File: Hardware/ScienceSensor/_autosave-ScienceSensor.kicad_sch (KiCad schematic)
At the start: 16 parts

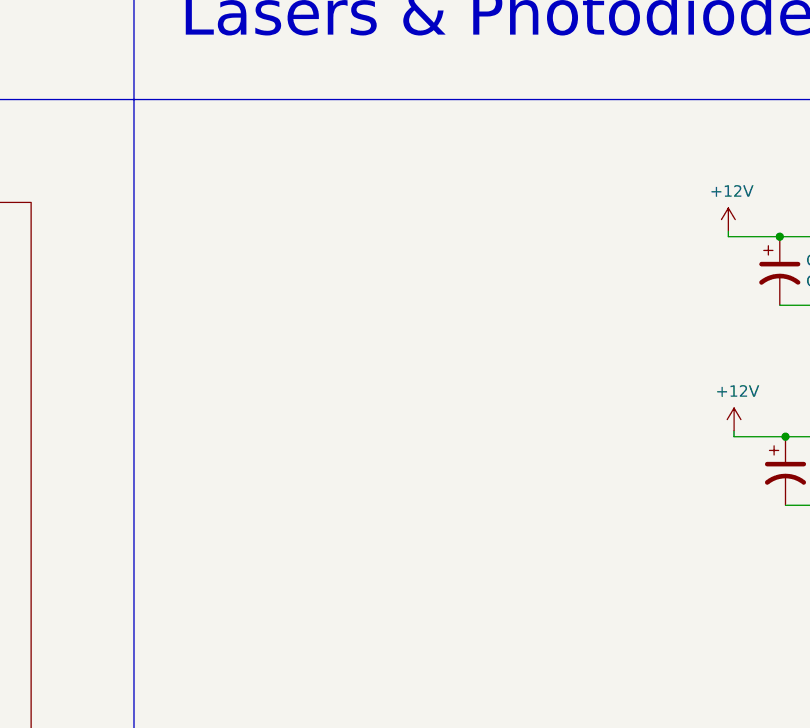
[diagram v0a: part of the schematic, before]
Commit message: Created servo and started limit switch for microscope.
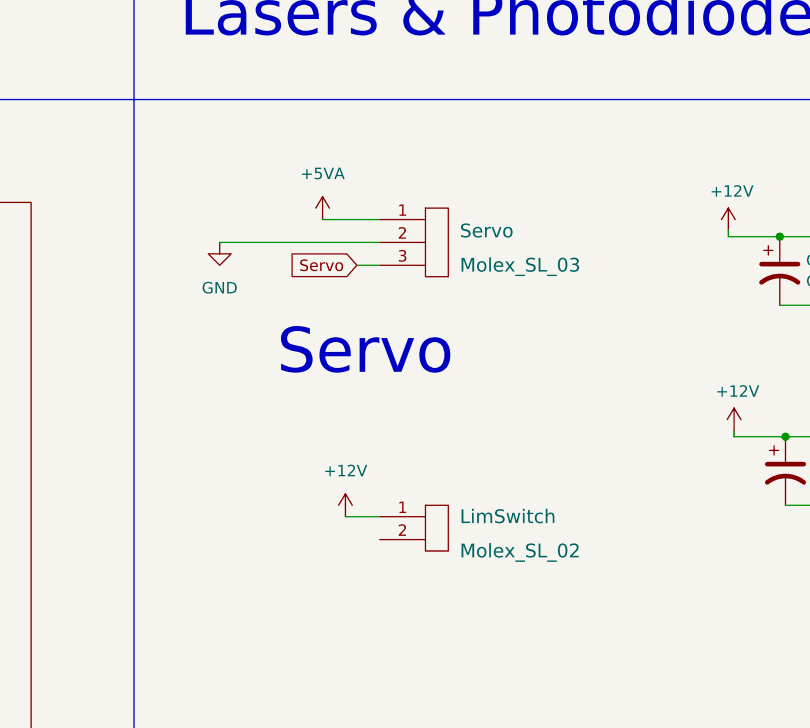
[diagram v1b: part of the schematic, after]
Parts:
- added LimSwitch: Molex_SL_02, symbol MRDT_Connectors:Molex_SL_02
- added Servo: Molex_SL_03, symbol MRDT_Connectors:Molex_SL_03
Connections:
- net +12V: now also LimSwitch.1
- net GND: now also Servo.2
- new net +5VA: Servo.1
- new net Servo: Servo.3
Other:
- note added: "Servo"
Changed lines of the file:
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@@
+    (stroke (width 0) (type default) (color 0 0 0 0))
+  )
+  (wire (pts (xy 140.97 115.57) (xy 147.32 115.57))
     (stroke (width 0) (type default) (color 0 0 0 0))
   )
@@
     (stroke (width 0) (type default) (color 0 0 0 0))
   )
+  (wire (pts (xy 143.51 148.59) (xy 147.32 148.59))
+    (stroke (width 0) (type default) (color 0 0 0 0))
+  )
   (wire (pts (xy 186.69 139.7) (xy 186.69 139.065))
     (stroke (width 0) (type default) (color 0 0 0 0))
@@
   )
   (polyline (pts (xy 209.55 59.69) (xy 284.48 59.69))
+    (stroke (width 0) (type default) (color 0 0 0 0))
+  )
+  (wire (pts (xy 129.54 118.11) (xy 147.32 118.11))
+    (stroke (width 0) (type default) (color 0 0 0 0))
+  )
+  (wire (pts (xy 144.78 120.65) (xy 147.32 120.65))
     (stroke (width 0) (type default) (color 0 0 0 0))
   )
@@
     (effects (font (size 5.0038 5.0038)) (justify left bottom))
   )
+  (text "Servo" (at 135.89 133.35 0)
+    (effects (font (size 5 5)) (justify left bottom))
+  )
   (text "OKIs" (at 218.44 163.195 0)
     (effects (font (size 5.0038 5.0038)) (justify left bottom))
@@
   (text "Lasers & Photodiode" (at 125.095 95.885 0)
     (effects (font (size 5.0038 5.0038)) (justify left bottom))
+  )
+  (global_label "Servo" (shape input) (at 144.78 120.65 180) (fields_autoplaced)
+    (effects (font (size 1.27 1.27)) (justify right))
+    (property "Intersheet References" "${INTERSHEET_REFS}" (id 0) (at 137.2548 120.5706 0)
+      (effects (font (size 1.27 1.27)) (justify right) hide)
+    )
   )
   (symbol (lib_id "MRDT_Connectors:AndersonPP") (at 217.805 38.735 0) (unit 1)
@@
     )
     (property "Datasheet" "" (id 3) (at 273.05 146.685 0)
+      (effects (font (size 1.27 1.27)) hide)
+    )
+    (pin "1")
+  )
+  (symbol (lib_id "power:+5VA") (at 140.97 115.57 0) (unit 1)
+    (in_bom yes) (on_board yes) (fields_autoplaced)
+    (property "Reference" "#PWR?" (id 0) (at 140.97 119.38 0)
+      (effects (font (size 1.27 1.27)) hide)
+    )
+    (property "Value" "+5VA" (id 1) (at 140.97 110.49 0))
+    (property "Footprint" "" (id 2) (at 140.97 115.57 0)
+      (effects (font (size 1.27 1.27)) hide)
+    )
+    (property "Datasheet" "" (id 3) (at 140.97 115.57 0)
+      (effects (font (size 1.27 1.27)) hide)
+    )
+    (pin "1")
+  )
+  (symbol (lib_id "MRDT_Connectors:Molex_SL_02") (at 152.4 152.4 0) (unit 1)
+    (in_bom yes) (on_board yes) (fields_autoplaced)
+    (property "Reference" "LimSwitch" (id 0) (at 156.21 148.59 0)
+      (effects (font (size 1.524 1.524)) (justify left))
+    )
+    (property "Value" "Molex_SL_02" (id 1) (at 156.21 152.4 0)
+      (effects (font (size 1.524 1.524)) (justify left))
+    )
+    (property "Footprint" "" (id 2) (at 152.4 154.94 0)
+      (effects (font (size 1.524 1.524)) hide)
+    )
+    (property "Datasheet" "" (id 3) (at 152.4 154.94 0)
+      (effects (font (size 1.524 1.524)) hide)
+    )
+    (pin "1")
+    (pin "2")
+  )
+  (symbol (lib_id "power:+12V") (at 143.51 148.59 0) (unit 1)
+    (in_bom yes) (on_board yes) (fields_autoplaced)
+    (property "Reference" "#PWR?" (id 0) (at 143.51 152.4 0)
+      (effects (font (size 1.27 1.27)) hide)
+    )
+    (property "Value" "+12V" (id 1) (at 143.51 143.51 0))
+    (property "Footprint" "" (id 2) (at 143.51 148.59 0)
+      (effects (font (size 1.27 1.27)) hide)
+    )
+    (property "Datasheet" "" (id 3) (at 143.51 148.59 0)
+      (effects (font (size 1.27 1.27)) hide)
+    )
+    (pin "1")
+  )
+  (symbol (lib_id "MRDT_Connectors:Molex_SL_03") (at 152.4 121.92 0) (unit 1)
+    (in_bom yes) (on_board yes) (fields_autoplaced)
+    (property "Reference" "Servo" (id 0) (at 156.21 116.84 0)
+      (effects (font (size 1.524 1.524)) (justify left))
+    )
+    (property "Value" "Molex_SL_03" (id 1) (at 156.21 120.65 0)
+      (effects (font (size 1.524 1.524)) (justify left))
+    )
+    (property "Footprint" "" (id 2) (at 152.4 121.92 0)
+      (effects (font (size 1.524 1.524)) hide)
+    )
+    (property "Datasheet" "" (id 3) (at 152.4 121.92 0)
+      (effects (font (size 1.524 1.524)) hide)
+    )
+    (pin "1")
+    (pin "2")
+    (pin "3")
+  )
+  (symbol (lib_id "power:GND") (at 129.54 118.11 0) (unit 1)
+    (in_bom yes) (on_board yes) (fields_autoplaced)
+    (property "Reference" "#PWR?" (id 0) (at 129.54 124.46 0)
+      (effects (font (size 1.27 1.27)) hide)
+    )
+    (property "Value" "GND" (id 1) (at 129.54 123.19 0))
+    (property "Footprint" "" (id 2) (at 129.54 118.11 0)
+      (effects (font (size 1.27 1.27)) hide)
+    )
+    (property "Datasheet" "" (id 3) (at 129.54 118.11 0)
       (effects (font (size 1.27 1.27)) hide)
     )
@@
       (reference "#PWR?") (unit 1) (value "GND") (footprint "")
     )
+    (path "/36c3c08d-4146-41e4-94b7-044f09c961cb"
+      (reference "#PWR?") (unit 1) (value "+5VA") (footprint "")
+    )
     (path "/00000000-0000-0000-0000-00006320eb63/3e7ed085-3cd4-4f6d-8202-15727f978cdf"
       (reference "#PWR?") (unit 1) (value "GND") (footprint "")
@@
       (reference "#PWR?") (unit 1) (value "GND") (footprint "")
     )
+    (path "/901edaad-e3b4-4c7b-a659-8e096758971e"
+      (reference "#PWR?") (unit 1) (value "+12V") (footprint "")
+    )
     (path "/00000000-0000-0000-0000-00006320eb63/a103f583-b944-4021-ad5f-ca2f4caf3b45"
       (reference "#PWR?") (unit 1) (value "+5V") (footprint "")
@@
       (reference "#PWR?") (unit 1) (value "+3V3") (footprint "")
     )
+    (path "/bf7f8f1d-4d0e-4846-95e2-0af30ff15873"
+      (reference "#PWR?") (unit 1) (value "GND") (footprint "")
+    )
     (path "/00000000-0000-0000-0000-00006320eb63/d1b2d36e-b22f-4855-8066-df1268014de7"
       (reference "#PWR?") (unit 1) (value "+5V") (footprint "")
@@
       (reference "J?") (unit 1) (value "6P6C") (footprint "")
     )
+    (path "/8ae2a257-be4b-4a10-bade-909438328e71"
+      (reference "LimSwitch") (unit 1) (value "Molex_SL_02") (footprint "")
+    )
     (path "/00000000-0000-0000-0000-00006320eb63/9d7b7ebb-5a71-429c-9cd2-3189b799a8ec"
       (reference "Q1") (unit 1) (value "BSS138") (footprint "")
@@
       (reference "R?") (unit 1) (value "R") (footprint "")
     )
+    (path "/b4a915a0-b6dc-4ffb-b797-f39e8f562123"
+      (reference "Servo") (unit 1) (value "Molex_SL_03") (footprint "")
+    )
     (path "/00000000-0000-0000-0000-00006320eb63/4361c90c-dd26-46c6-b314-bdbe49286a65"
